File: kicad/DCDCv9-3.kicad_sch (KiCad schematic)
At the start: 187 parts, among them J1 Screw_Terminal_01x03, J1.1 Screw_Terminal_01x03, J1.2 Screw_Terminal_01x03, J2 Conn_01x02_Male, J3 Conn_01x02, J3.1 Conn_01x02, J3.2 Conn_01x01_Pin, J3.3 Conn_01x01_Pin, J4 Conn_01x02_Male, J5 XT60 Male, J5.1 XT60 Female (wrong symbol ik), J6 Conn_01x02_Male, J7 Conn_01x02_Male, J8 Conn_01x02_Male, M1 Fan, Q1 PMV20ENR, Q10 IMBG65R050M2HXTMA1, Q11 IMBG65R050M2HXTMA1, Q2 PMV20ENR, Q3 SIHP24N80AE-GE3, Q4 IXYP8N90C3, Q5 PMV20ENR, Q6 PMV20ENR, Q7 PMV20ENR, T1 DIY Transformer ETD 39, T1.1 Ferrite Core, T1.2 Ferrite Core (gapped), T1.3 1800 mm 120 x 0.1 mm HF litz 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, T1.4 165 mm 600 x 0,071 mm HF litz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, T1.5 165 mm 600 x 0,071 mm HF litz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, U1 TBA 1-1212HI, U10 LM2904BIDDFR, U11 UCC21520DW, U12 UCC25600, U13 ZXRE330ASA-7, U14 LM2904BIDDFR, U2 RT9058-90GVL, U3 MP4541_SOP8-EP, U4 TLV61048DBVR, U6 LM2904BIDDFR, U7 TL431, U9 ACPL-217-50AE

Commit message: updated bom, wrong 22uF cap for 0805 footprint
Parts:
- C12, C18, C27, C42, C54, C8: Manufacturer_Part_Number GRM188C61E226ME01J -> CL21A226MAYNNNE
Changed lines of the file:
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@@
 	(label "OTP_FAN"
 		(at 135.89 262.89 180)
-		(fields_autoplaced yes)
 		(effects
 			(font
@@
 	(label "OVP"
 		(at 285.75 89.535 0)
-		(fields_autoplaced yes)
 		(effects
 			(font
@@
 	(label "OC"
 		(at 254 53.975 0)
-		(fields_autoplaced yes)
 		(effects
 			(font
@@
 	(label "HS"
 		(at 275.59 53.975 180)
-		(fields_autoplaced yes)
 		(effects
 			(font
@@
 	(label "OC"
 		(at 144.78 147.32 0)
-		(fields_autoplaced yes)
 		(effects
 			(font
@@
 	(label "Opc+"
 		(at 343.535 123.19 0)
-		(fields_autoplaced yes)
 		(effects
 			(font
@@
 	(label "UVP"
 		(at 267.97 89.535 0)
-		(fields_autoplaced yes)
 		(effects
 			(font
@@
 	(label "OTP_OFF"
 		(at 78.74 262.89 180)
-		(fields_autoplaced yes)
 		(effects
 			(font
@@
 	(label "OVP"
 		(at 386.08 46.99 180)
-		(fields_autoplaced yes)
 		(effects
 			(font
@@
 	(label "LS"
 		(at 57.15 142.24 0)
-		(fields_autoplaced yes)
 		(effects
 			(font
@@
 	(label "OTP_OFF"
 		(at 226.06 219.71 0)
-		(fields_autoplaced yes)
 		(effects
 			(font
@@
 	(label "Opc+"
 		(at 239.395 35.56 270)
-		(fields_autoplaced yes)
 		(effects
 			(font
@@
 	(label "LS"
 		(at 275.59 64.135 180)
-		(fields_autoplaced yes)
 		(effects
 			(font
@@
 	(label "HB_out"
 		(at 137.16 137.16 0)
-		(fields_autoplaced yes)
 		(effects
 			(font
@@
 	(label "OTP_FAN"
 		(at 243.84 219.71 0)
-		(fields_autoplaced yes)
 		(effects
 			(font
@@
 	(label "UVP"
 		(at 353.06 46.99 180)
-		(fields_autoplaced yes)
 		(effects
 			(font
@@
 	(label "HS"
 		(at 57.15 139.7 0)
-		(fields_autoplaced yes)
 		(effects
 			(font
@@
 			)
 		)
-		(property "Datasheet" "https://www.mouser.de/ProductDetail/Murata-Electronics/GRM188C61E226ME01J?qs=Z%252BL2brAPG1Ka41zYia00qA%3D%3D"
+		(property "Datasheet" "https://www.mouser.de/ProductDetail/Samsung-Electro-Mechanics/CL21A226MAYNNNE?qs=xZ%2FP%252Ba9zWqY%2FVvCfXjMhqg%3D%3D"
 			(at 186.69 214.63 0)
 			(effects
@@
 			)
 		)
-		(property "Manufacturer_Part_Number" "GRM188C61E226ME01J"
+		(property "Manufacturer_Part_Number" "CL21A226MAYNNNE"
 			(at 186.69 214.63 0)
 			(effects
@@
 			)
 		)
-		(property "Datasheet" "https://www.mouser.de/ProductDetail/Murata-Electronics/GRM188C61E226ME01J?qs=Z%252BL2brAPG1Ka41zYia00qA%3D%3D"
+		(property "Datasheet" "https://www.mouser.de/ProductDetail/Samsung-Electro-Mechanics/CL21A226MAYNNNE?qs=xZ%2FP%252Ba9zWqY%2FVvCfXjMhqg%3D%3D"
 			(at 92.71 220.345 0)
 			(effects
@@
 			)
 		)
-		(property "Manufacturer_Part_Number" "GRM188C61E226ME01J"
+		(property "Manufacturer_Part_Number" "CL21A226MAYNNNE"
 			(at 92.71 220.345 0)
 			(effects
@@
 			)
 		)
-		(property "Datasheet" "https://www.mouser.de/ProductDetail/Murata-Electronics/GRM188C61E226ME01J?qs=Z%252BL2brAPG1Ka41zYia00qA%3D%3D"
+		(property "Datasheet" "https://www.mouser.de/ProductDetail/Samsung-Electro-Mechanics/CL21A226MAYNNNE?qs=xZ%2FP%252Ba9zWqY%2FVvCfXjMhqg%3D%3D"
 			(at 229.235 73.025 0)
 			(effects
@@
 			)
 		)
-		(property "Manufacturer_Part_Number" "GRM188C61E226ME01J"
+		(property "Manufacturer_Part_Number" "CL21A226MAYNNNE"
 			(at 229.235 73.025 0)
 			(effects
@@
 			)
 		)
-		(property "Datasheet" "https://www.mouser.de/ProductDetail/Murata-Electronics/GRM188C61E226ME01J?qs=Z%252BL2brAPG1Ka41zYia00qA%3D%3D"
+		(property "Datasheet" "https://www.mouser.de/ProductDetail/Samsung-Electro-Mechanics/CL21A226MAYNNNE?qs=xZ%2FP%252Ba9zWqY%2FVvCfXjMhqg%3D%3D"
 			(at 193.04 214.63 0)
 			(effects
@@
 			)
 		)
-		(property "Manufacturer_Part_Number" "GRM188C61E226ME01J"
+		(property "Manufacturer_Part_Number" "CL21A226MAYNNNE"
 			(at 193.04 214.63 0)
 			(effects
@@
 			)
 		)
-		(property "Datasheet" "https://www.mouser.de/ProductDetail/Murata-Electronics/GRM188C61E226ME01J?qs=Z%252BL2brAPG1Ka41zYia00qA%3D%3D"
+		(property "Datasheet" "https://www.mouser.de/ProductDetail/Samsung-Electro-Mechanics/CL21A226MAYNNNE?qs=xZ%2FP%252Ba9zWqY%2FVvCfXjMhqg%3D%3D"
 			(at 129.54 220.345 0)
 			(effects
@@
 			)
 		)
-		(property "Manufacturer_Part_Number" "GRM188C61E226ME01J"
+		(property "Manufacturer_Part_Number" "CL21A226MAYNNNE"
 			(at 129.54 220.345 0)
 			(effects
@@
 			)
 		)
-		(property "Datasheet" "https://www.mouser.de/ProductDetail/Murata-Electronics/GRM188C61E226ME01J?qs=Z%252BL2brAPG1Ka41zYia00qA%3D%3D"
+		(property "Datasheet" "https://www.mouser.de/ProductDetail/Samsung-Electro-Mechanics/CL21A226MAYNNNE?qs=xZ%2FP%252Ba9zWqY%2FVvCfXjMhqg%3D%3D"
 			(at 133.35 220.345 0)
 			(effects
@@
 			)
 		)
-		(property "Manufacturer_Part_Number" "GRM188C61E226ME01J"
+		(property "Manufacturer_Part_Number" "CL21A226MAYNNNE"
 			(at 133.35 220.345 0)
 			(effects

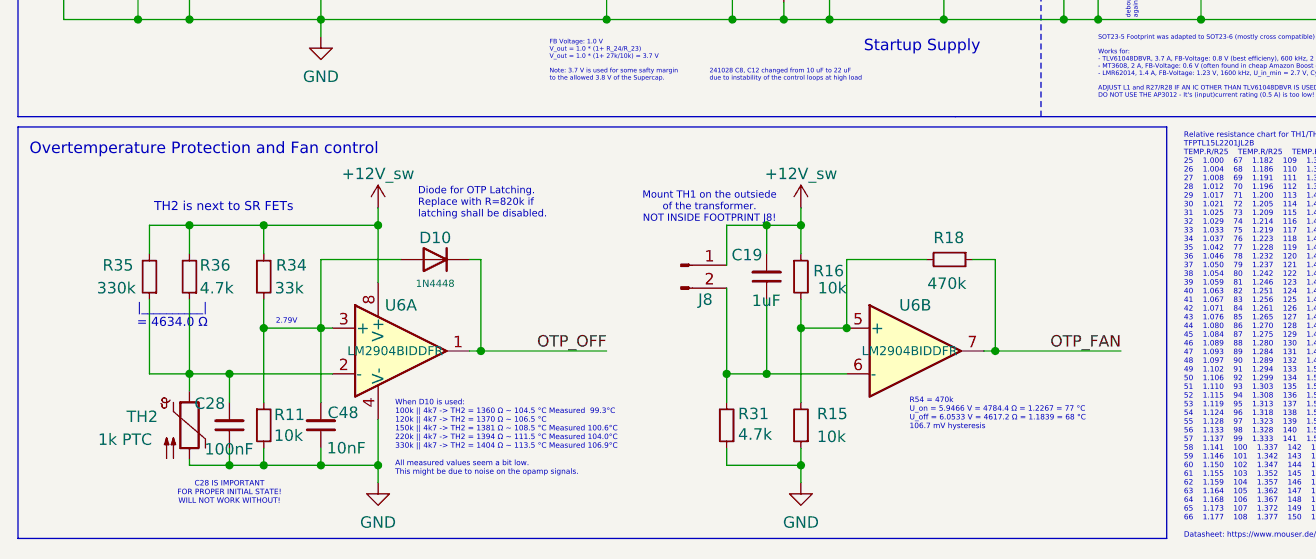
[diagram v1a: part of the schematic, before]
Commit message: Added R75 to lower the fan turn-on temperature
Note: R75 (100k) is not added in the PCB design due to space restrictions. It is paralleled to R31 (4.7k) so the parallel value is around 4.49 k. The turn-on temperature is now 72°C and turn-off 58°C.
The original design was measured to have 71°C/61°C on/off. However it was found that when mounted, the transformer could reach 90°C on the top without turning on the fan. A new measurement showed, that it actually turned on at 84°C and 70°C off, but everything else (e.g. voltages) seem to be the same from the initial measurement. There might be a bias due to the initial value being measured without being mounted to the transformer. Anyways, the lowered threshold will prolong the component's lifetime due to lower thermal stress. Soldering R75 on top of R31 is recommended but not 100% needed.
Replacing R31 with 4.3 k is possible too, but the fan will probably run all the time due to an even lower turn on/off threshold.
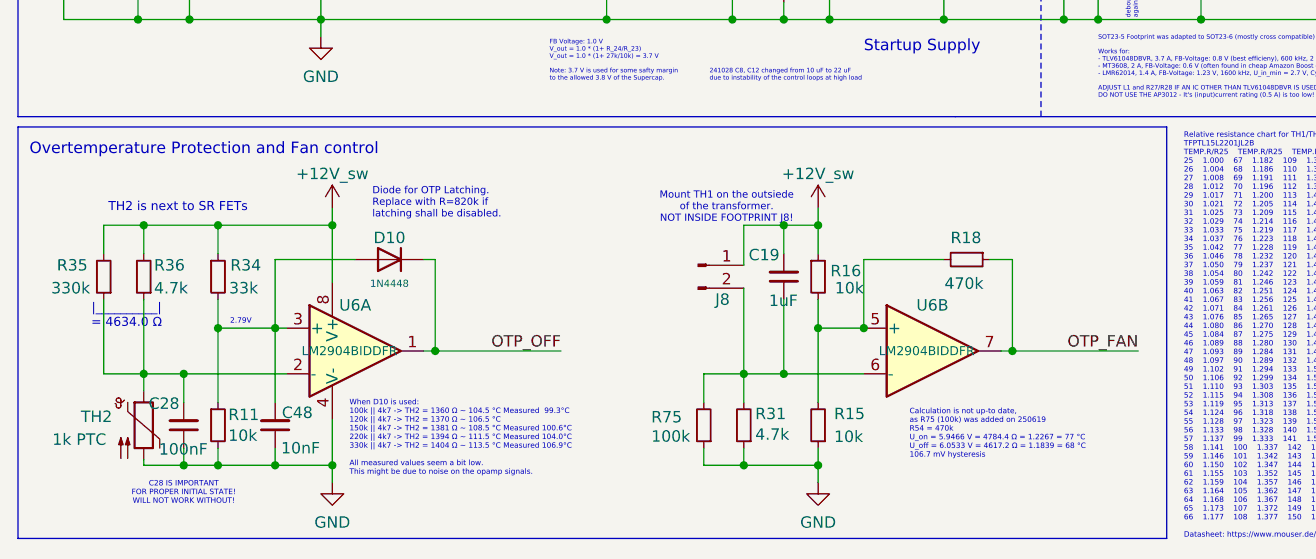
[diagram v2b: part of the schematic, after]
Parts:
- added R75: 100k, DCDC-Footprints:R_0603_1608Metric, symbol Device:R_Small
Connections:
- net GND: now also R75.1
- net at C19.1, J8.2 (Pin_2), R31.2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: now also R75.2
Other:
- note added: "Calculation is not up-to date, as R75 (100k) was added on 250619 R54 = 470k U_on = 5.9466 V = 4784.4 Ω = 1.2267 = 77 °C U_off = 6.0533 V = 4617.2 Ω = 1.1839 = 68 °C 106.7 mV hysteresis"
- note removed: "R54 = 470k U_on = 5.9466 V = 4784.4 Ω = 1.2267 = 77 °C U_off = 6.0533 V = 4617.2 Ω = 1.1839 = 68 °C 106.7 mV hysteresis"
- moved on the sheet: C19, C28, C48, D10, J8, R11, R15, R16, R18, R31, R34, R35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

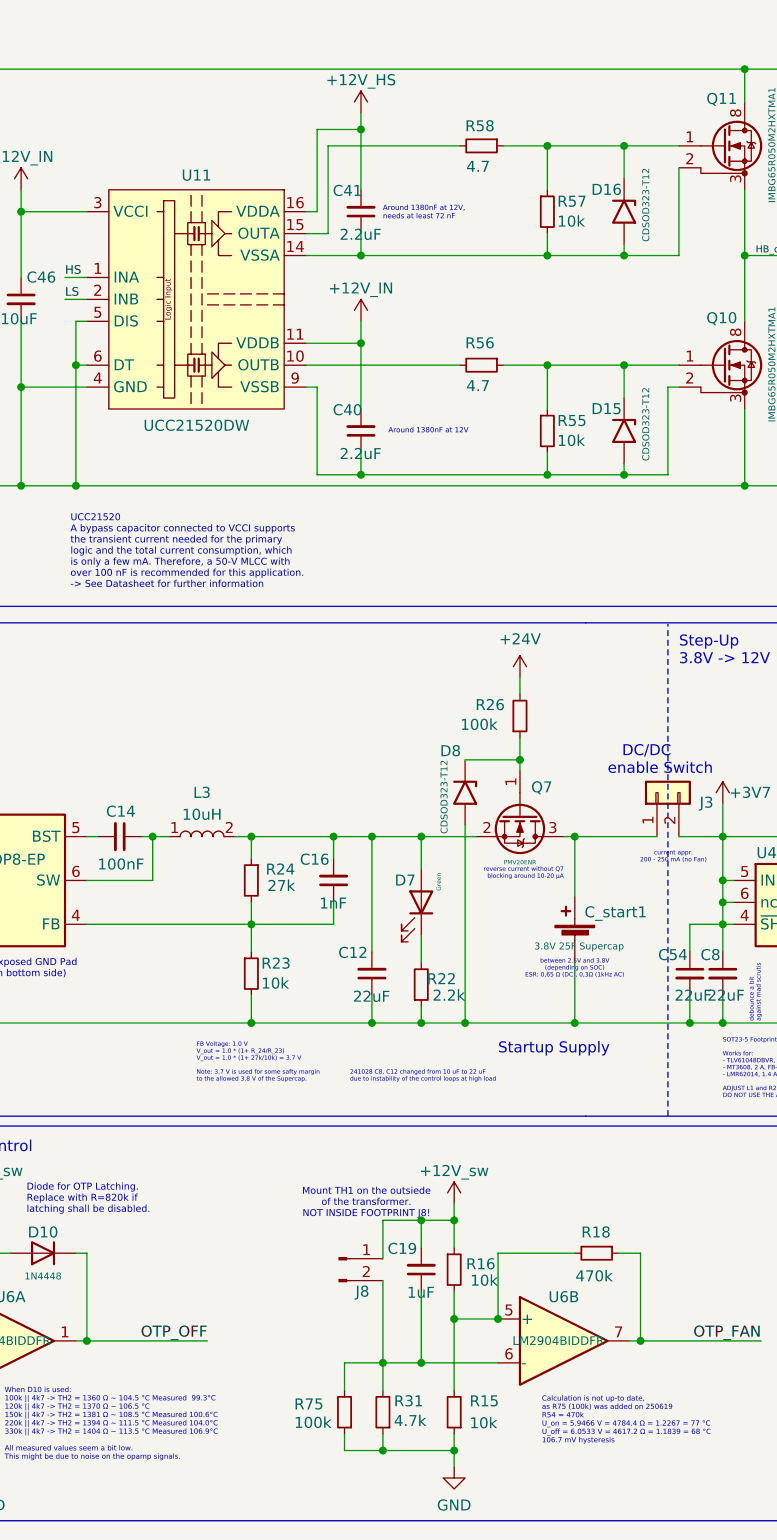
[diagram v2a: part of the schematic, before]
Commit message: Important update: Changed Gate Resistors
R58 and R56 have been changed due to slight overvoltage. Deadtime must be increased to at least 150 ns (turn RV1 CCW). For more details see release notes DCDCv9-3r1.3
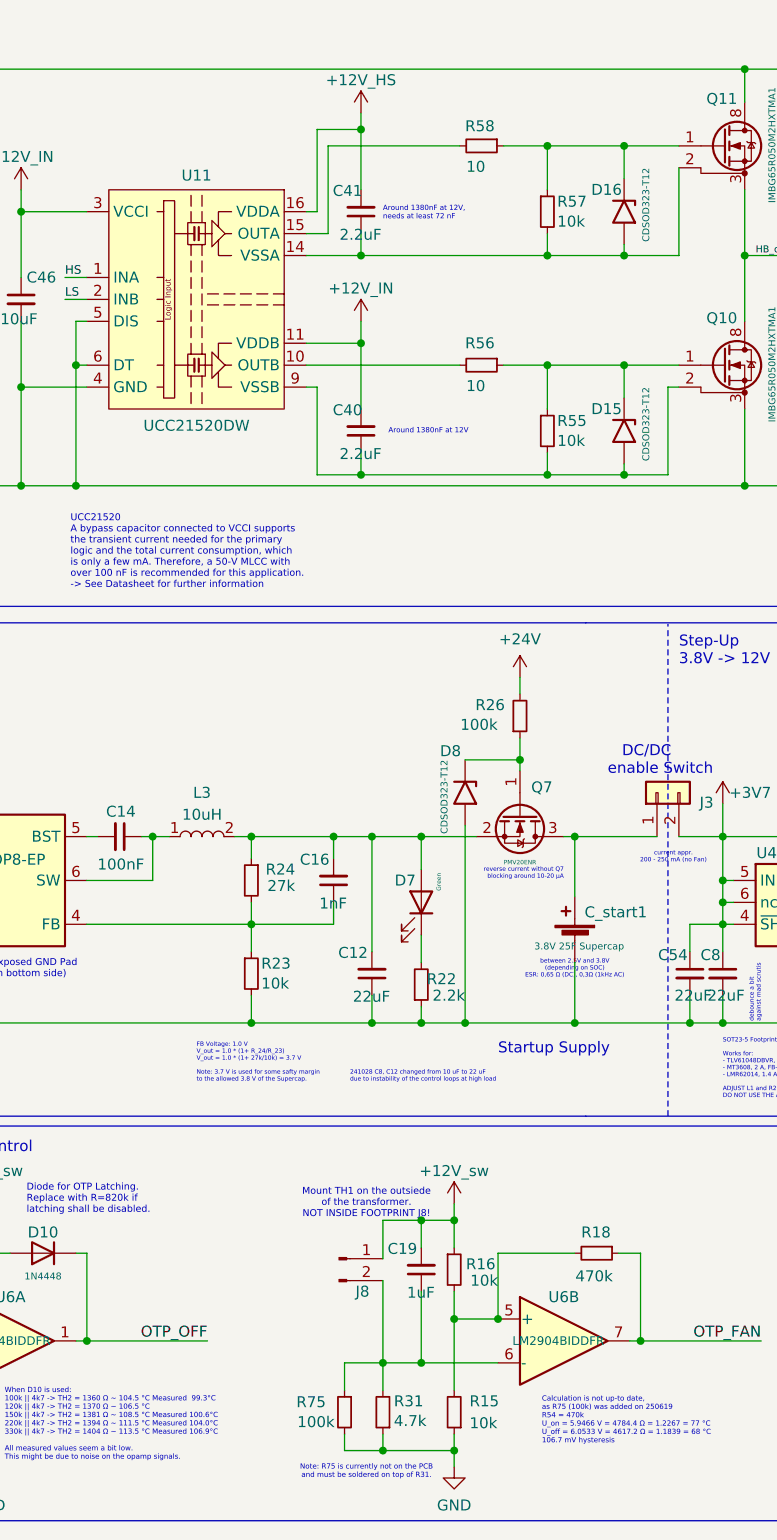
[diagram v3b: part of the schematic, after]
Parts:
- R56, R58: value 4.7 -> 10; Manufacturer_Part_Number ERJ-P08J4R7V -> RC1206FR-7W10RL
- R75: footprint DCDC-Footprints:R_0603_1608Metric -> Resistor_SMD:R_0603_1608Metric; comment Voltage divider with R52, but also pull-up when Precharge i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 -> Note: R75 is currently not on the PCB and must be soldered 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; ignore for iBom 1 -> (none)
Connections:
- net GND: now also R75.2; no longer R75.1
- net at C19.1, J8.2 (Pin_2), R31.2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: now also R75.1; no longer R75.2
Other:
- note added: "Note: R75 is currently not on the PCB and must be soldered on top of R31."
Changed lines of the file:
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@@
 	(title_block
 		(title "DC/DC v9-3r1")
-		(date "2025-03-16")
+		(date "2025-06-29")
 		(company "Author: Rootthecause")
 	)
@@
 		)
 	)
+	(text "Note: R75 is currently not on the PCB \nand must be soldered on top of R31. "
+		(exclude_from_sim no)
+		(at 92.075 278.13 0)
+		(effects
+			(font
+				(size 0.6 0.6)
+			)
+		)
+	)
 	(text "Test points LV"
 		(exclude_from_sim no)
@@
 	)
 	(symbol
+		(lib_id "Device:R_Small")
+		(at 89.535 271.145 0)
+		(mirror y)
+		(unit 1)
+		(exclude_from_sim no)
+		(in_bom yes)
+		(on_board yes)
+		(dnp no)
+		(property "Reference" "R75"
+			(at 87.376 269.9766 0)
+			(effects
+				(font
+					(size 1.27 1.27)
+				)
+				(justify left)
+			)
+		)
+		(property "Value" "100k"
+			(at 88.392 272.288 0)
+			(effects
+				(font
+					(size 1.27 1.27)
+				)
+				(justify left)
+			)
+		)
+		(property "Footprint" "Resistor_SMD:R_0603_1608Metric"
+			(at 89.535 271.145 0)
+			(effects
+				(font
+					(size 1.27 1.27)
+				)
+				(hide yes)
+			)
+		)
+		(property "Datasheet" "https://www.mouser.de/ProductDetail/ROHM-Semiconductor/ESR03EZPJ104?qs=493kPxzlxfLd9svH5sC01g%3D%3D"
+			(at 89.535 271.145 0)
+			(effects
+				(font
+					(size 1.27 1.27)
+				)
+				(hide yes)
+			)
+		)
+		(property "Description" ""
+			(at 89.535 271.145 0)
+			(effects
+				(font
+					(size 1.27 1.27)
+				)
+				(hide yes)
+			)
+		)
+		(property "Manufacturer_Part_Number" "ESR03EZPJ104"
+			(at 89.535 271.145 0)
+			(effects
+				(font
+					(size 1.27 1.27)
+				)
+				(hide yes)
+			)
+		)
+		(property "Qty Order" "5"
+			(at 89.535 271.145 0)
+			(effects
+				(font
+					(size 1.27 1.27)
+				)
+				(hide yes)
+			)
+		)
+		(property "ignore for iBom" ""
+			(at 89.535 271.145 0)
+			(effects
+				(font
+					(size 1.27 1.27)
+				)
+				(hide yes)
+			)
+		)
+		(property "comment" "Note: R75 is currently not on the PCB  and must be soldered on top of R31. "
+			(at 89.535 271.145 0)
+			(effects
+				(font
+					(size 1.27 1.27)
+				)
+				(hide yes)
+			)
+		)
+		(property "Source" "Mouser"
+			(at 89.535 271.145 0)
+			(effects
+				(font
+					(size 1.27 1.27)
+				)
+				(hide yes)
+			)
+		)
+		(pin "1"
+		)
+		(pin "2"
+		)
+		(instances
+			(project "DCDCv9-3"
+				(path "/e63e39d7-6ac0-4ffd-8aa3-1841a4541b55"
+					(reference "R75")
+					(unit 1)
+				)
+			)
+		)
+	)
+	(symbol
 		(lib_id "Device:C_Small")
 		(at 320.04 142.875 180)
@@
 			)
 		)
-		(property "Value" "4.7"
+		(property "Value" "10"
 			(at 103.632 152.273 90)
 			(effects
@@
 			)
 		)
-		(property "Datasheet" "https://www.mouser.de/ProductDetail/Panasonic/ERJ-P08J4R7V?qs=sGAEpiMZZMtlubZbdhIBIK7FbVYKWV6WtRy9y9o9OQM%3D"
+		(property "Datasheet" "https://www.mouser.de/ProductDetail/YAGEO/RC1206FR-7W10RL?qs=tggtontpCXM7RQCPv1SaRw%3D%3D"
 			(at 105.41 149.86 0)
 			(effects
@@
 			)
 		)
-		(property "Manufacturer_Part_Number" "ERJ-P08J4R7V"
+		(property "Manufacturer_Part_Number" "RC1206FR-7W10RL"
 			(at 105.41 149.86 0)
 			(effects
@@
 			)
 		)
-		(property "Value" "4.7"
+		(property "Value" "10"
 			(at 103.632 126.873 90)
 			(effects
@@
 			)
 		)
-		(property "Datasheet" "https://www.mouser.de/ProductDetail/Panasonic/ERJ-P08J4R7V?qs=sGAEpiMZZMtlubZbdhIBIK7FbVYKWV6WtRy9y9o9OQM%3D"
+		(property "Datasheet" "https://www.mouser.de/ProductDetail/YAGEO/RC1206FR-7W10RL?qs=tggtontpCXM7RQCPv1SaRw%3D%3D"
 			(at 105.41 124.46 0)
 			(effects
@@
 			)
 		)
-		(property "Manufacturer_Part_Number" "ERJ-P08J4R7V"
+		(property "Manufacturer_Part_Number" "RC1206FR-7W10RL"
 			(at 105.41 124.46 0)
 			(effects
@@
 					(unit 1)
 				)
-			)
-		)
-	)
-	(symbol
-		(lib_id "Device:R_Small")
-		(at 89.535 271.145 180)
-		(unit 1)
-		(exclude_from_sim no)
-		(in_bom yes)
-		(on_board yes)
-		(dnp no)
-		(property "Reference" "R75"
-			(at 83.693 270.2365 0)
-			(effects
-				(font
-					(size 1.27 1.27)
-				)
-				(justify right)
-			)
-		)
-		(property "Value" "100k"
-			(at 83.693 272.3766 0)
-			(effects
-				(font
-					(size 1.27 1.27)
-				)
-				(justify right)
-			)
-		)
-		(property "Footprint" "DCDC-Footprints:R_0603_1608Metric"
-			(at 89.535 271.145 0)
-			(effects
-				(font
-					(size 1.27 1.27)
-				)
-				(hide yes)
-			)
-		)
-		(property "Datasheet" "https://www.mouser.de/ProductDetail/ROHM-Semiconductor/ESR03EZPJ104?qs=493kPxzlxfLd9svH5sC01g%3D%3D"
-			(at 89.535 271.145 0)
-			(effects
-				(font
-					(size 1.27 1.27)
-				)
-				(hide yes)
-			)
-		)
-		(property "Description" ""
-			(at 89.535 271.145 0)
-			(effects
-				(font
-					(size 1.27 1.27)
-				)
-				(hide yes)
-			)
-		)
-		(property "Manufacturer_Part_Number" "ESR03EZPJ104"
-			(at 89.535 271.145 0)
-			(effects
-				(font
-					(size 1.27 1.27)
-				)
-				(hide yes)
-			)
-		)
-		(property "Qty Order" "5"
-			(at 89.535 271.145 0)
-			(effects
-				(font
-					(size 1.27 1.27)
-				)
-				(hide yes)
-			)
-		)
-		(property "ignore for iBom" "1"
-			(at 89.535 271.145 0)
-			(effects
-				(font
-					(size 1.27 1.27)
-				)
-				(hide yes)
-			)
-		)
-		(property "comment" "Voltage divider with R52, but also pull-up when Precharge is not done"
-			(at 89.535 271.145 0)
-			(effects
-				(font
-					(size 1.27 1.27)
-				)
-				(hide yes)
-			)
-		)
-		(property "Source" "Mouser"
-			(at 89.535 271.145 0)
-			(effects
-				(font
-					(size 1.27 1.27)
-				)
-				(hide yes)
-			)
-		)
-		(pin "1"
-		)
-		(pin "2"
-		)
-		(instances
-			(project "DCDCv9-3"
-				(path "/e63e39d7-6ac0-4ffd-8aa3-1841a4541b55"
-					(reference "R75")
-					(unit 1)
-				)

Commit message: IMPORTANT NOTICE see #10 and fix in iBom
IMPORTANT NOTICE: There was a complaint about the converter not being rules conform. Due to other personal priorities it might take some weeks to solve the addressed points. There is also the chance of some points unable to be resolved. See #10 for further details.
iBom: There were some components missing in the iBom for PCBA.
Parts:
- C12, C14, C15, C16, C17, C18, C19, C2, C20, C21, C22, C23, C24, C26, C27, C28, C29, C3, C30, C32, C33, C38, C39, C40, C41, C42, C43, C44, C45, C46, C47, C48, C49, C5, C50, C51, C52, C53, C54, C55, C56, C57, C8, D1, D10, D13, D15, D16, D17, D18, D2, D3, D4, D5, D6, D7, D8, D9, J6, J7, Q1, Q2, Q5, Q6, Q7, R1, R10, R11, R12, R15, R16, R17, R18, R2, R21, R22, R23, R24, R25, R26, R27, R28, R3, R31, R34, R35, R36, R37, R39, R4, R41, R44, R45, R46, R47, R48, R49, R5, R50, R51, R52, R53, R54, R55, R56, R57, R58, R59, R6, R60, R61, R62, R63, R64, R65, R66, R67, R68, R69, R7, R70, R71, R72, R73, R74, R8, R9, U10, U11, U12, U14, U4, U6, U7, U9: ignore for iBOM (none) -> 1; ignore for iBom 1 -> (none)
- RV1, RV2: ignore for iBom 1 -> (none)
- T1: ignore for PCBA 1 -> (none)
- T1.3, T1.4, T1.5: ignore for PCBA (none) -> 1
